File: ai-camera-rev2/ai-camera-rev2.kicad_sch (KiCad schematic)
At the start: 174 parts, among them J1 Conn-01x02_P2mm_NONAME_JST-PH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, J2 TYPE-C-31-M-12, J3 DBG, J4 Conn-02x10_P2.54mm_B-2100S20P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, J5 Conn-01x02_P1.25mm_10114829-1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, J6 Conn_01x24_FFC_0.5mm_AFC01-S2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, Q1 2N7002, Q2 2N7002, Q3 AO3401A, Q4 AO3401A, Q5 2N7002, Q6 AO3401A, Q7 2N7002, Q8 AO3401A, Q9 2N7002, SW1 SW_PB_90deg_K2-1102AQ-H4CW-01, SW2 SW_PB_TS-1187A-B-A-B, SW3 SW_PB_TS-1187A-B-A-B, SW4 SW_PB_90deg_K2-1102AQ-H4CW-01, U1 TP4057-42-SOT26-R, U10 ESP32-S3-WROOM-1-N16R8, U11 MT9284-28J, U12 LTR-303ALS-01, U2 XC6206-2.8V, U3 PCF85063AT_SO8, U4 SOT-23-6_SN74LVC1G373DBVR_TI, U5 SY8089AAAC, U6 PIR_AS312, U7 XC6206-2.8V, U8 RT9166-12GVL, U9 AP1511B, Y1 32.768kHz_Q13FC1350000400

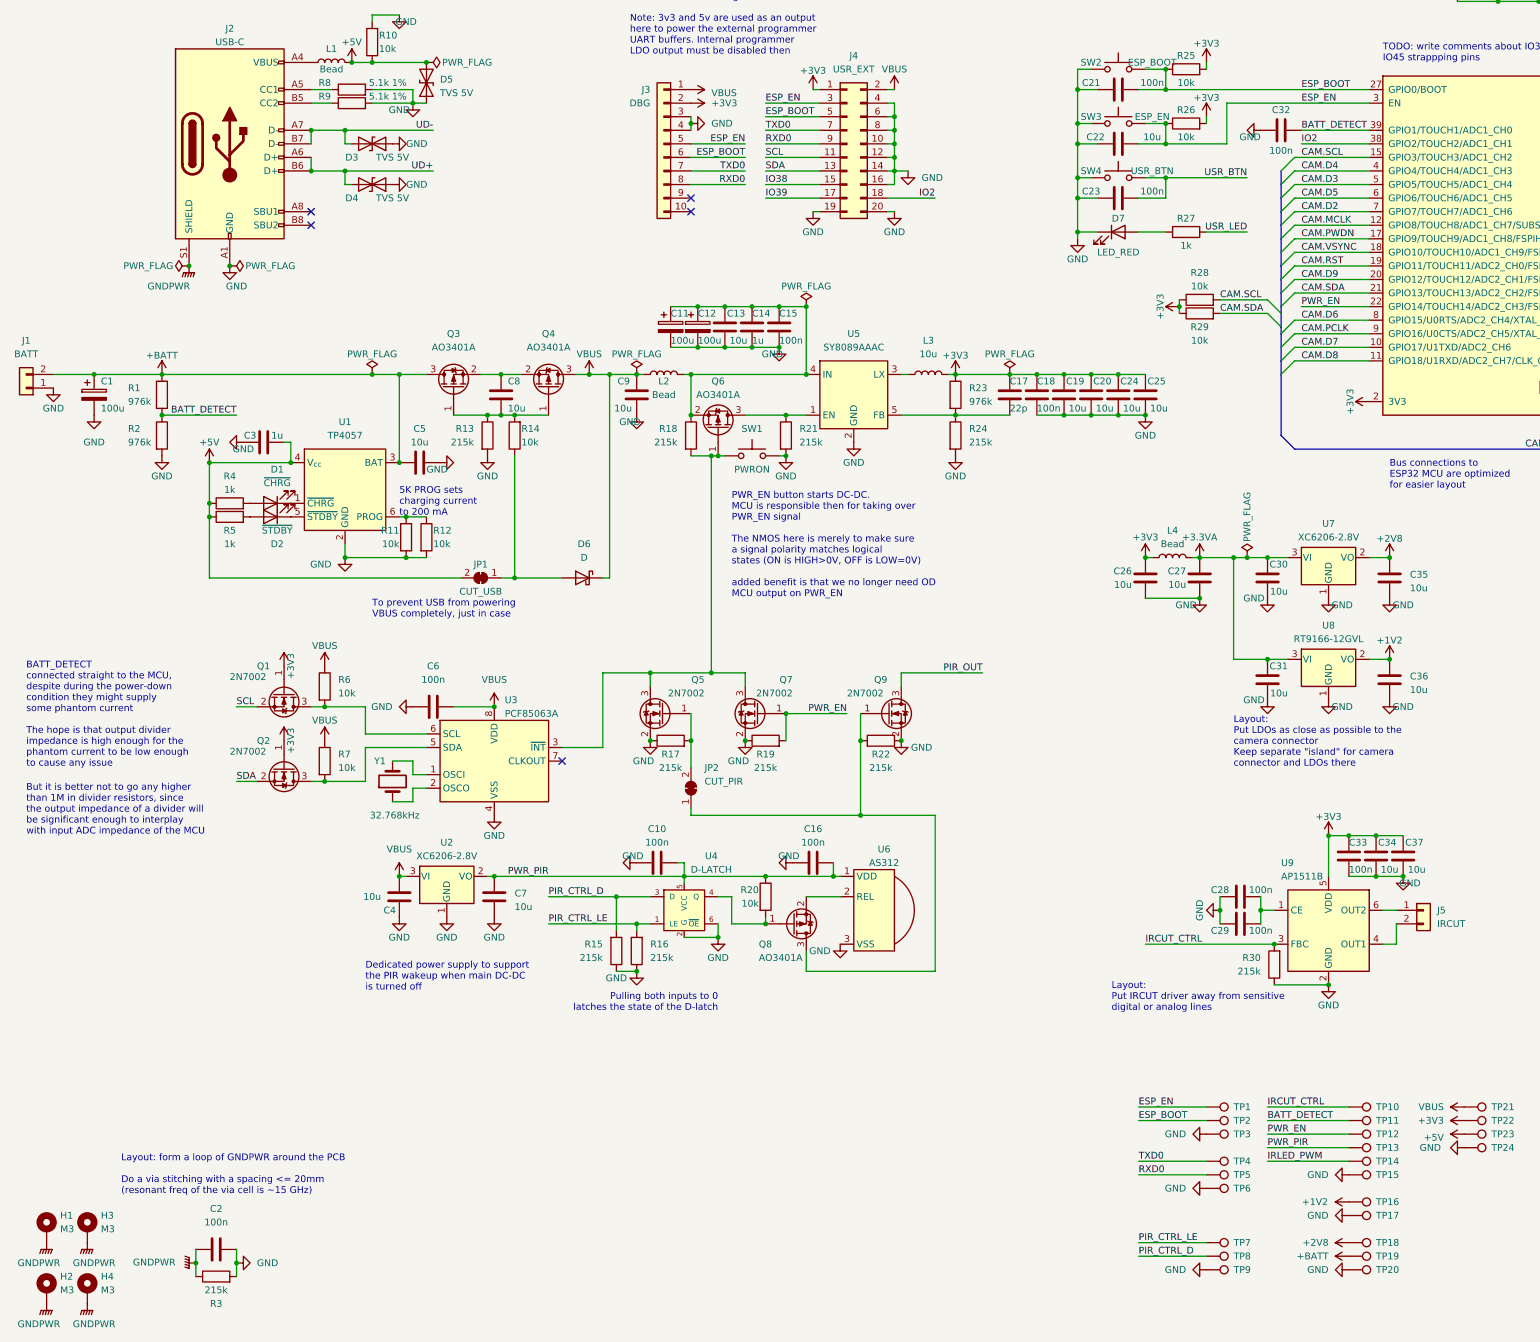
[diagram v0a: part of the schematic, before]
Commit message: EAC-49: update schematics for newest library symbols
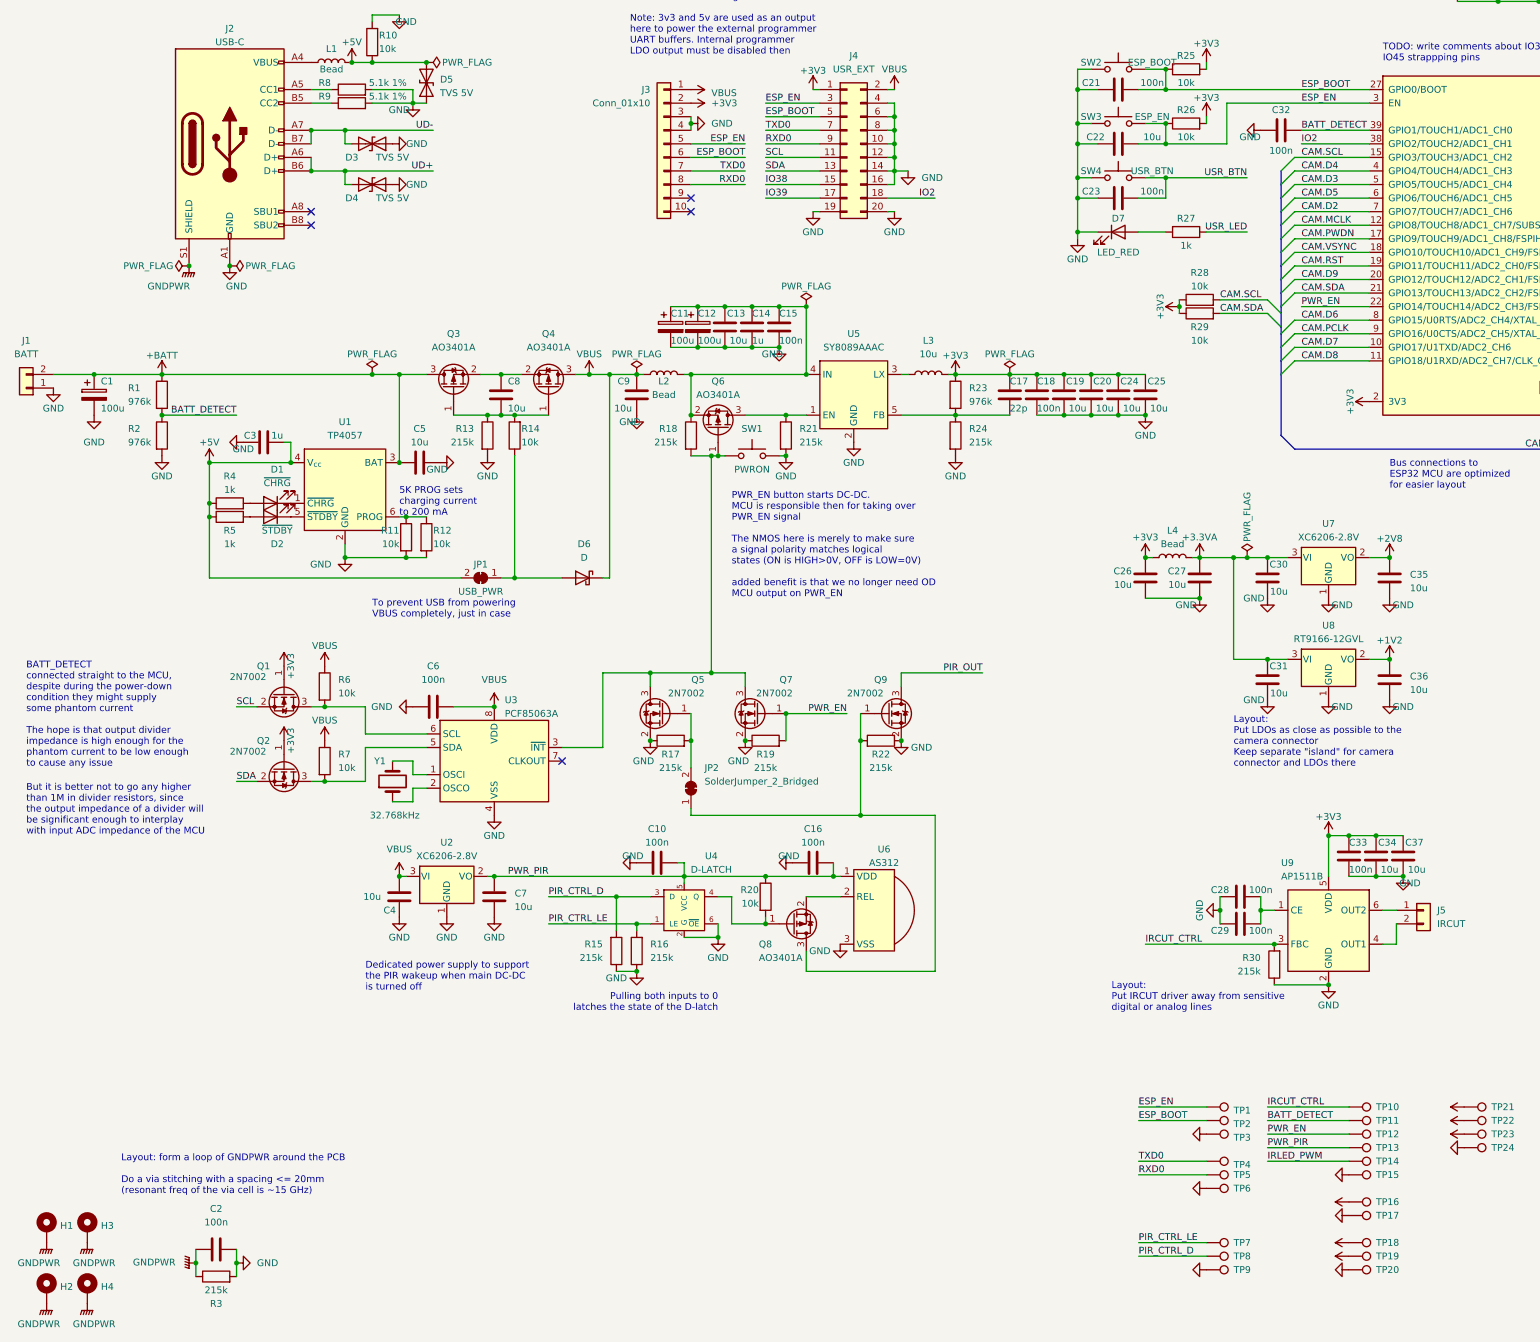
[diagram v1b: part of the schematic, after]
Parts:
- H1, H2, H3, H4: value M3 -> MountingHole_Pad; footprint MountingHole:MountingHole_3.2mm_M3_DIN965_Pad_TopBottom -> (none); now in the parts list
- J3: value DBG -> Conn_01x10; footprint Connector:Tag-Connect_TC2050-IDC-NL_2x05_P1.27mm_Vertical -> (none); now in the parts list
- JP1: value CUT_USB -> USB_PWR; footprint Jumper:SolderJumper-2_P1.3mm_Bridged_RoundedPad1.0x1.5mm -> (none); now in the parts list
- JP2: value CUT_PIR -> SolderJumper_2_Bridged; footprint Jumper:SolderJumper-2_P1.3mm_Bridged_RoundedPad1.0x1.5mm -> (none); now in the parts list
- Q1, Q2, Q5, Q7, Q9: symbol 00-kiml-transitor-fet:2N7002 -> 00-kiml-transistor-fet:2N7002
- Q3, Q4, Q6, Q8: symbol 00-kiml-transitor-fet:AO3401A -> 00-kiml-transistor-fet:AO3401A
- TP1, TP10, TP11, TP12, TP13, TP14, TP15, TP16, TP17, TP18, TP19, TP2, TP20, TP21, TP22, TP23, TP24, TP3, TP4, TP5, TP6, TP7, TP8, TP9: value TP -> TestPoint; footprint TestPoint:TestPoint_Pad_D1.5mm -> (none); now in the parts list

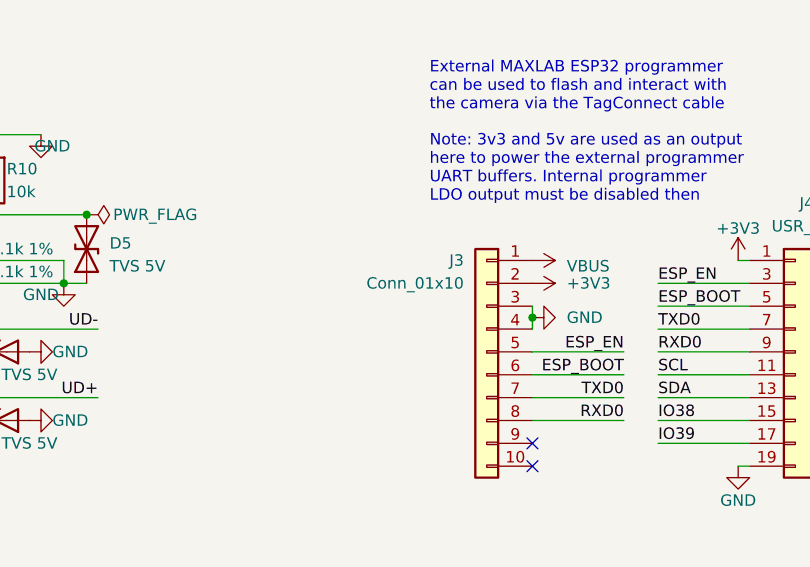
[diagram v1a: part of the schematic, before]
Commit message: EAC-49: move ALS, PIR and improve power routing
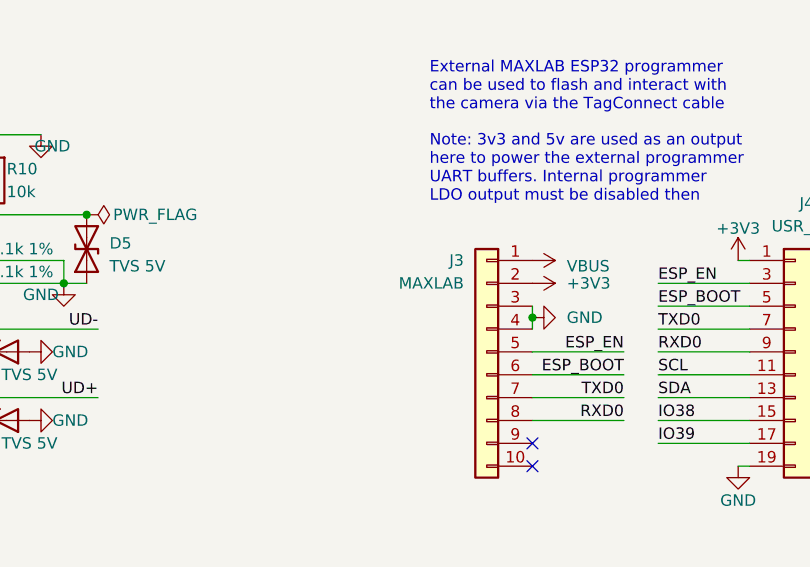
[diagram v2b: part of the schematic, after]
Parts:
- H1, H2, H3, H4: footprint (none) -> MountingHole:MountingHole_3.2mm_M3_Pad_TopBottom
- J3: value Conn_01x10 -> MAXLAB; footprint (none) -> Connector:Tag-Connect_TC2050-IDC-FP_2x05_P1.27mm_Vertical
- JP1, JP2: footprint (none) -> Jumper:SolderJumper-2_P1.3mm_Bridged2Bar_Pad1.0x1.5mm
- TP1, TP10, TP11, TP12, TP13, TP14, TP15, TP16, TP17, TP18, TP19, TP2, TP20, TP21, TP22, TP23, TP24, TP3, TP4, TP5, TP6, TP7, TP8, TP9: footprint (none) -> TestPoint:TestPoint_Pad_D1.0mm
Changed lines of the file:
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@@
       (effects (font (size 1.27 1.27)) (justify left) hide)
     )
-    (property "Footprint" "" (at 285.75 251.46 0)
+    (property "Footprint" "TestPoint:TestPoint_Pad_D1.0mm" (at 285.75 251.46 0)
       (effects (font (size 1.27 1.27)) hide)
     )
@@
       (effects (font (size 1.27 1.27)) (justify left) hide)
     )
-    (property "Footprint" "" (at 237.49 259.08 0)
+    (property "Footprint" "TestPoint:TestPoint_Pad_D1.0mm" (at 237.49 259.08 0)
       (effects (font (size 1.27 1.27)) hide)
     )
@@
       (effects (font (size 1.27 1.27)) (justify left) hide)
     )
-    (property "Footprint" "" (at 237.49 246.38 0)
+    (property "Footprint" "TestPoint:TestPoint_Pad_D1.0mm" (at 237.49 246.38 0)
       (effects (font (size 1.27 1.27)) hide)
     )
@@
       (effects (font (size 1.27 1.27)) (justify left) hide)
     )
-    (property "Footprint" "" (at 264.16 274.32 0)
+    (property "Footprint" "TestPoint:TestPoint_Pad_D1.0mm" (at 264.16 274.32 0)
       (effects (font (size 1.27 1.27)) hide)
     )
@@
       (effects (font (size 1.27 1.27)) (justify left) hide)
     )
-    (property "Footprint" "" (at 237.49 254 0)
+    (property "Footprint" "TestPoint:TestPoint_Pad_D1.0mm" (at 237.49 254 0)
       (effects (font (size 1.27 1.27)) hide)
     )
@@
       (effects (font (size 1.27 1.27)) (justify left) hide)
     )
-    (property "Footprint" "" (at 237.49 243.84 0)
+    (property "Footprint" "TestPoint:TestPoint_Pad_D1.0mm" (at 237.49 243.84 0)
       (effects (font (size 1.27 1.27)) hide)
     )
@@
       (effects (font (size 1.27 1.27)) (justify left) hide)
     )
-    (property "Footprint" "" (at 237.49 271.78 0)
+    (property "Footprint" "TestPoint:TestPoint_Pad_D1.0mm" (at 237.49 271.78 0)
       (effects (font (size 1.27 1.27)) hide)
     )
@@
       (effects (font (size 1.27 1.27)) (justify left) hide)
     )
-    (property "Footprint" "" (at 237.49 269.24 0)
+    (property "Footprint" "TestPoint:TestPoint_Pad_D1.0mm" (at 237.49 269.24 0)
       (effects (font (size 1.27 1.27)) hide)
     )
@@
       (effects (font (size 1.27 1.27)) (justify left) hide)
     )
-    (property "Footprint" "" (at 20.32 261.62 0)
+    (property "Footprint" "MountingHole:MountingHole_3.2mm_M3_Pad_TopBottom" (at 20.32 261.62 0)
       (effects (font (size 1.27 1.27)) hide)
     )
@@
       (effects (font (size 1.27 1.27)) (justify left) hide)
     )
-    (property "Footprint" "" (at 237.49 248.92 0)
+    (property "Footprint" "TestPoint:TestPoint_Pad_D1.0mm" (at 237.49 248.92 0)
       (effects (font (size 1.27 1.27)) hide)
     )
@@
       (effects (font (size 1.27 1.27)) (justify left) hide)
     )
-    (property "Footprint" "" (at 264.16 269.24 0)
+    (property "Footprint" "TestPoint:TestPoint_Pad_D1.0mm" (at 264.16 269.24 0)
       (effects (font (size 1.27 1.27)) hide)
     )
@@
       (effects (font (size 1.27 1.27)) (justify left) hide)
     )
-    (property "Footprint" "" (at 264.16 243.84 0)
+    (property "Footprint" "TestPoint:TestPoint_Pad_D1.0mm" (at 264.16 243.84 0)
       (effects (font (size 1.27 1.27)) hide)
     )
@@
       (effects (font (size 1.27 1.27)) (justify left) hide)
     )
-    (property "Footprint" "" (at 264.16 264.16 0)
+    (property "Footprint" "TestPoint:TestPoint_Pad_D1.0mm" (at 264.16 264.16 0)
       (effects (font (size 1.27 1.27)) hide)
     )
@@
       (effects (font (size 1.27 1.27)) (justify left) hide)
     )
-    (property "Footprint" "" (at 285.75 243.84 0)
+    (property "Footprint" "TestPoint:TestPoint_Pad_D1.0mm" (at 285.75 243.84 0)
       (effects (font (size 1.27 1.27)) hide)
     )
@@
       (effects (font (size 1.27 1.27)) (justify left) hide)
     )
-    (property "Footprint" "" (at 27.94 261.62 0)
+    (property "Footprint" "MountingHole:MountingHole_3.2mm_M3_Pad_TopBottom" (at 27.94 261.62 0)
       (effects (font (size 1.27 1.27)) hide)
     )
@@
       (effects (font (size 1.27 1.27)) (justify left) hide)
     )
-    (property "Footprint" "" (at 264.16 254 0)
+    (property "Footprint" "TestPoint:TestPoint_Pad_D1.0mm" (at 264.16 254 0)
       (effects (font (size 1.27 1.27)) hide)
     )
@@
       (effects (font (size 1.27 1.27)))
     )
-    (property "Footprint" "" (at 101.6 139.7 0)
+    (property "Footprint" "Jumper:SolderJumper-2_P1.3mm_Bridged2Bar_Pad1.0x1.5mm" (at 101.6 139.7 0)
       (effects (font (size 1.27 1.27)) hide)
     )
@@
       (effects (font (size 1.27 1.27)) (justify left) hide)
     )
-    (property "Footprint" "" (at 237.49 274.32 0)
+    (property "Footprint" "TestPoint:TestPoint_Pad_D1.0mm" (at 237.49 274.32 0)
       (effects (font (size 1.27 1.27)) hide)
     )
@@
       (effects (font (size 1.27 1.27)) (justify left) hide)
     )
-    (property "Footprint" "" (at 264.16 261.62 0)
+    (property "Footprint" "TestPoint:TestPoint_Pad_D1.0mm" (at 264.16 261.62 0)
       (effects (font (size 1.27 1.27)) hide)
     )
@@
       (effects (font (size 1.27 1.27)) (justify left) hide)
     )
-    (property "Footprint" "" (at 264.16 271.78 0)
+    (property "Footprint" "TestPoint:TestPoint_Pad_D1.0mm" (at 264.16 271.78 0)
       (effects (font (size 1.27 1.27)) hide)
     )
@@
       (effects (font (size 1.27 1.27)) (justify left) hide)
     )
-    (property "Footprint" "" (at 285.75 248.92 0)
+    (property "Footprint" "TestPoint:TestPoint_Pad_D1.0mm" (at 285.75 248.92 0)
       (effects (font (size 1.27 1.27)) hide)
     )
@@
       (effects (font (size 1.27 1.27)) (justify left))
     )
-    (property "Value" "Conn_01x10" (at 133.35 50.8 0)
+    (property "Value" "MAXLAB" (at 133.35 50.8 0)
       (effects (font (size 1.27 1.27)) (justify left))
     )
-    (property "Footprint" "" (at 135.89 58.42 0)
+    (property "Footprint" "Connector:Tag-Connect_TC2050-IDC-FP_2x05_P1.27mm_Vertical" (at 135.89 58.42 0)
       (effects (font (size 1.27 1.27)) hide)
     )
@@
       (effects (font (size 1.27 1.27)) (justify left) hide)
     )
-    (property "Footprint" "" (at 264.16 246.38 0)
+    (property "Footprint" "TestPoint:TestPoint_Pad_D1.0mm" (at 264.16 246.38 0)
       (effects (font (size 1.27 1.27)) hide)
     )
@@
       (effects (font (size 1.27 1.27)) (justify left) hide)
     )
-    (property "Footprint" "" (at 264.16 256.54 0)
+    (property "Footprint" "TestPoint:TestPoint_Pad_D1.0mm" (at 264.16 256.54 0)
       (effects (font (size 1.27 1.27)) hide)
     )
@@
       (effects (font (size 1.27 1.27)) (justify left) hide)
     )
-    (property "Footprint" "" (at 237.49 256.54 0)
+    (property "Footprint" "TestPoint:TestPoint_Pad_D1.0mm" (at 237.49 256.54 0)
       (effects (font (size 1.27 1.27)) hide)
     )
@@
       (effects (font (size 1.27 1.27)) (justify left) hide)
     )
-    (property "Footprint" "" (at 264.16 251.46 0)
+    (property "Footprint" "TestPoint:TestPoint_Pad_D1.0mm" (at 264.16 251.46 0)
       (effects (font (size 1.27 1.27)) hide)
     )
@@
       (effects (font (size 1.27 1.27)) (justify left) hide)
     )
-    (property "Footprint" "" (at 285.75 246.38 0)
+    (property "Footprint" "TestPoint:TestPoint_Pad_D1.0mm" (at 285.75 246.38 0)
       (effects (font (size 1.27 1.27)) hide)
     )
@@
       (effects (font (size 1.27 1.27)) (justify left) hide)
     )
-    (property "Footprint" "" (at 20.32 273.05 0)
+    (property "Footprint" "MountingHole:MountingHole_3.2mm_M3_Pad_TopBottom" (at 20.32 273.05 0)
       (effects (font (size 1.27 1.27)) hide)
     )
@@
       (effects (font (size 1.27 1.27)) (justify right))
     )
-    (property "Footprint" "" (at 140.97 179.07 0)
+    (property "Footprint" "Jumper:SolderJumper-2_P1.3mm_Bridged2Bar_Pad1.0x1.5mm" (at 140.97 179.07 0)
       (effects (font (size 1.27 1.27)) hide)
     )
@@
       (effects (font (size 1.27 1.27)) (justify left) hide)
     )
-    (property "Footprint" "" (at 264.16 248.92 0)
+    (property "Footprint" "TestPoint:TestPoint_Pad_D1.0mm" (at 264.16 248.92 0)
       (effects (font (size 1.27 1.27)) hide)
     )
@@
       (effects (font (size 1.27 1.27)) (justify left) hide)
     )
-    (property "Footprint" "" (at 27.94 273.05 0)
+    (property "Footprint" "MountingHole:MountingHole_3.2mm_M3_Pad_TopBottom" (at 27.94 273.05 0)
       (effects (font (size 1.27 1.27)) hide)
     )
